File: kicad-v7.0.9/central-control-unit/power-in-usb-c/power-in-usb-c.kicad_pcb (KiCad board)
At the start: 2 copper layers, 10.8 x 23.1 mm, 5 parts, among them P1 DS1021-1-4SF11-B

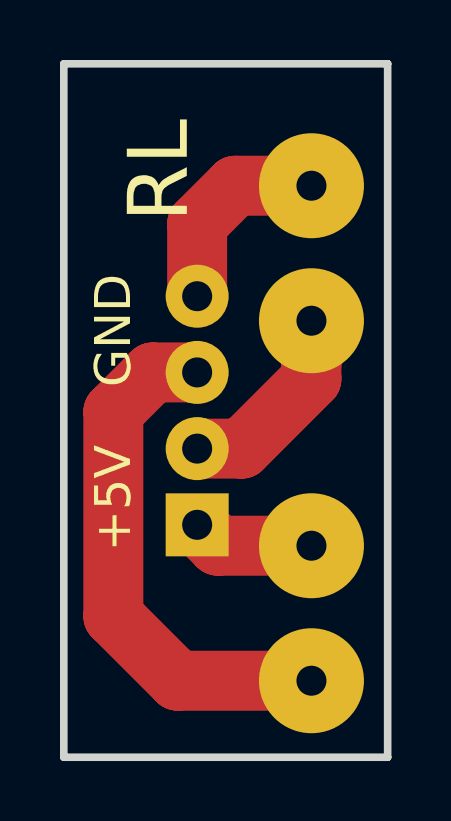
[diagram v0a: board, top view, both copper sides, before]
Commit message: Change components form library. Adding of BOM.
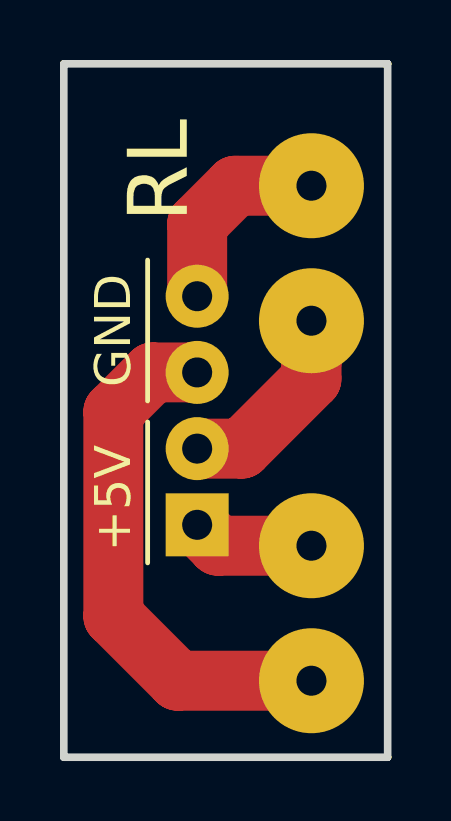
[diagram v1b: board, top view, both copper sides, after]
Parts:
- P1: footprint connector_tht_pinheader_2.54mm_rl:1x4_pinheader_2.54mm_vertical -> connector_pin_header_2.54mm_tht_rl:1x4_pin_header_2.54mm_vertical
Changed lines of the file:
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@@
     (descr "Mounting hole with pad 1 drill, 3.5 diameter")
     (tags "mountig hole pad 1x3.5")
-    (property "Sheetfile" "D:/kicad/thomas-thermostat/v2.0/kicad_v7/central-control-unit/v26_v1.0/power-in-usb-c/power-in-usb-c.sch")
+    (property "Sheetfile" "power-in-usb-c.kicad_sch")
     (property "Sheetname" "")
     (property "exclude_from_bom" "")
@@
     (descr "Mounting hole with pad 1 drill, 3.5 diameter")
     (tags "mountig hole pad 1x3.5")
-    (property "Sheetfile" "D:/kicad/thomas-thermostat/v2.0/kicad_v7/central-control-unit/v26_v1.0/power-in-usb-c/power-in-usb-c.sch")
+    (property "Sheetfile" "power-in-usb-c.kicad_sch")
     (property "Sheetname" "")
     (property "exclude_from_bom" "")
@@
     (descr "Mounting hole with pad 1 drill, 3.5 diameter")
     (tags "mountig hole pad 1x3.5")
-    (property "Sheetfile" "D:/kicad/thomas-thermostat/v2.0/kicad_v7/central-control-unit/v26_v1.0/power-in-usb-c/power-in-usb-c.sch")
+    (property "Sheetfile" "power-in-usb-c.kicad_sch")
     (property "Sheetname" "")
     (property "exclude_from_bom" "")
@@
     (descr "Mounting hole with pad 1 drill, 3.5 diameter")
     (tags "mountig hole pad 1x3.5")
-    (property "Sheetfile" "D:/kicad/thomas-thermostat/v2.0/kicad_v7/central-control-unit/v26_v1.0/power-in-usb-c/power-in-usb-c.sch")
+    (property "Sheetfile" "power-in-usb-c.kicad_sch")
     (property "Sheetname" "")
     (property "exclude_from_bom" "")
@@
       (net 1 "+5V") (pinfunction "1") (pintype "input"))
   )
-  (footprint "connector_tht_pinheader_2.54mm_rl:1x4_pinheader_2.54mm_vertical" (layer "B.Cu")
+  (footprint "connector_pin_header_2.54mm_tht_rl:1x4_pin_header_2.54mm_vertical" (layer "B.Cu")
     (at 179.07 79.883)
     (descr "Through hole straight pin header, 1x4, 2.54mm pitch, single row")
     (tags "Through hole pin header THT 1x4 2.54mm single row")
-    (property "Sheetfile" "D:/kicad/thomas-thermostat/v2.0/kicad_v7/central-control-unit/v26_v1.0/power-in-usb-c/power-in-usb-c.sch")
+    (property "Sheetfile" "power-in-usb-c.kicad_sch")
     (property "Sheetname" "")
     (property "ki_description" "1x4 pin header")
@@
     )
   )
+  (gr_line (start 177.419 76.454) (end 177.419 81.153)
+    (stroke (width 0.16) (type default)) (layer "F.SilkS"))
+  (gr_line (start 177.419 71.0565) (end 177.419 75.7555)
+    (stroke (width 0.16) (type default)) (layer "F.SilkS"))
   (gr_line (start 174.625 87.63) (end 174.625 64.516)
     (stroke (width 0.254) (type solid)) (layer "Edge.Cuts"))
